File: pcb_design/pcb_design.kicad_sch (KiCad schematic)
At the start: 4 parts, among them SW1 SW_Push, SW2 SW_Push, SW3 SW_Push, U1 MOUDLE-SEEEDUINO-XIAO

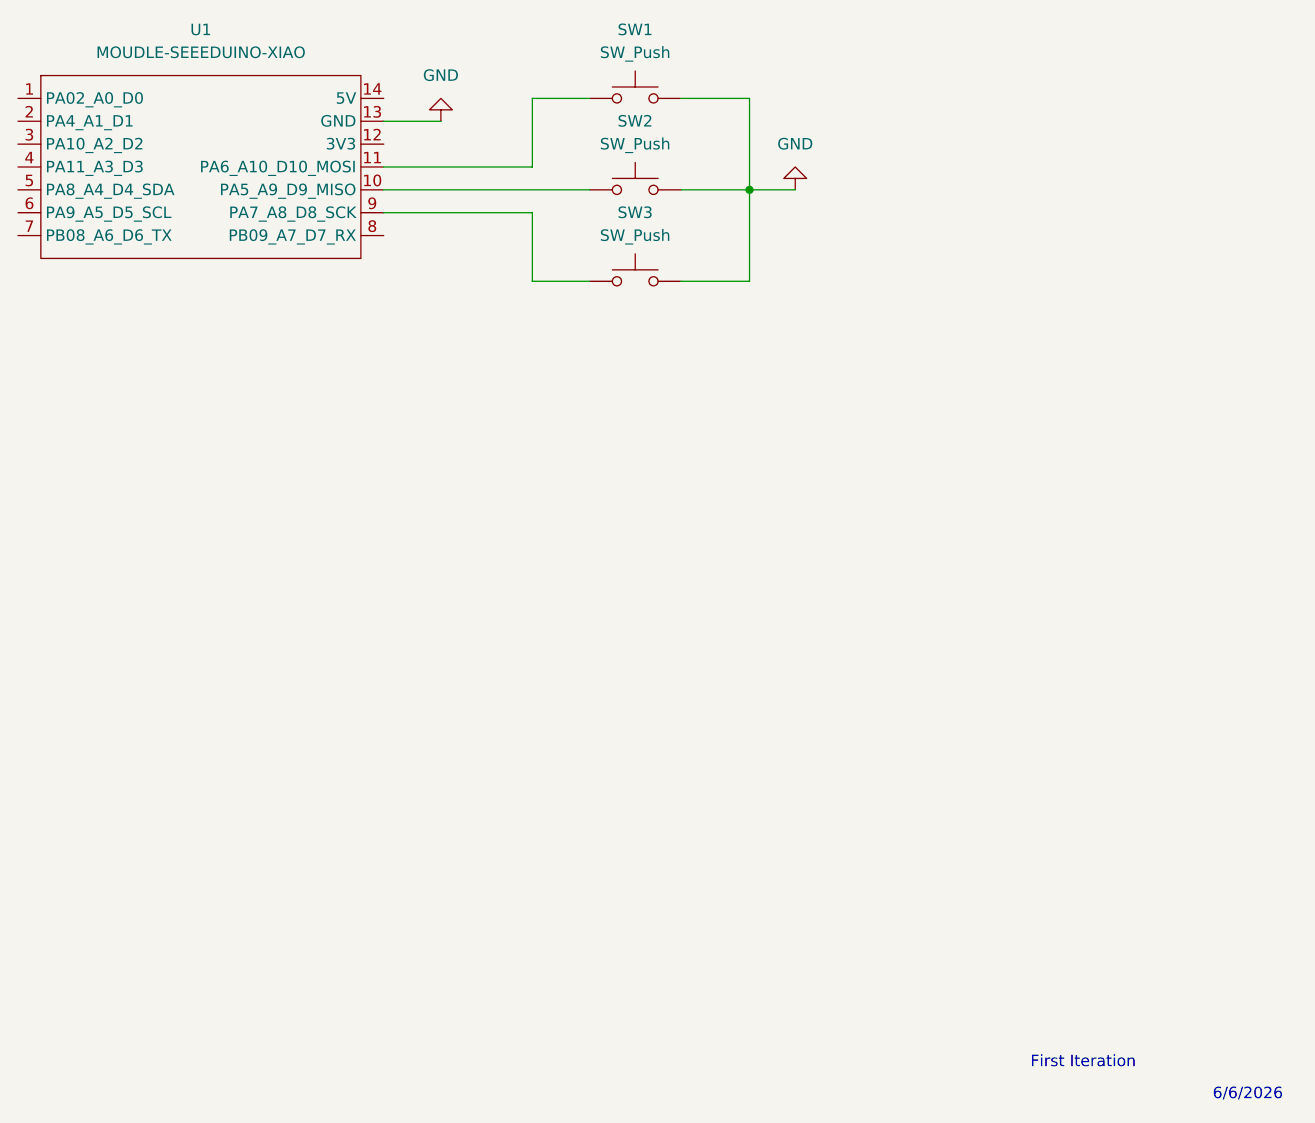
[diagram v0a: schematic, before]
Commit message: Finalized PCB Design.
1st Design Iteration - Followed the guide closely to understand the usage of KiCad.
2nd Design Iteration - Discovered the DRC function which let me fix some issues with the PCB Design
3rd Design Iteration - Redesigned the PCB to my own dimensions with a unique layout.
4th Design Iteration - Added an OLED Display to the hackpad and tested with encoder, but figured it wasn't serving a key role in my planned use case.
5th Design Iteration - Redesign the PCB to the newly discovered hackclub rules.
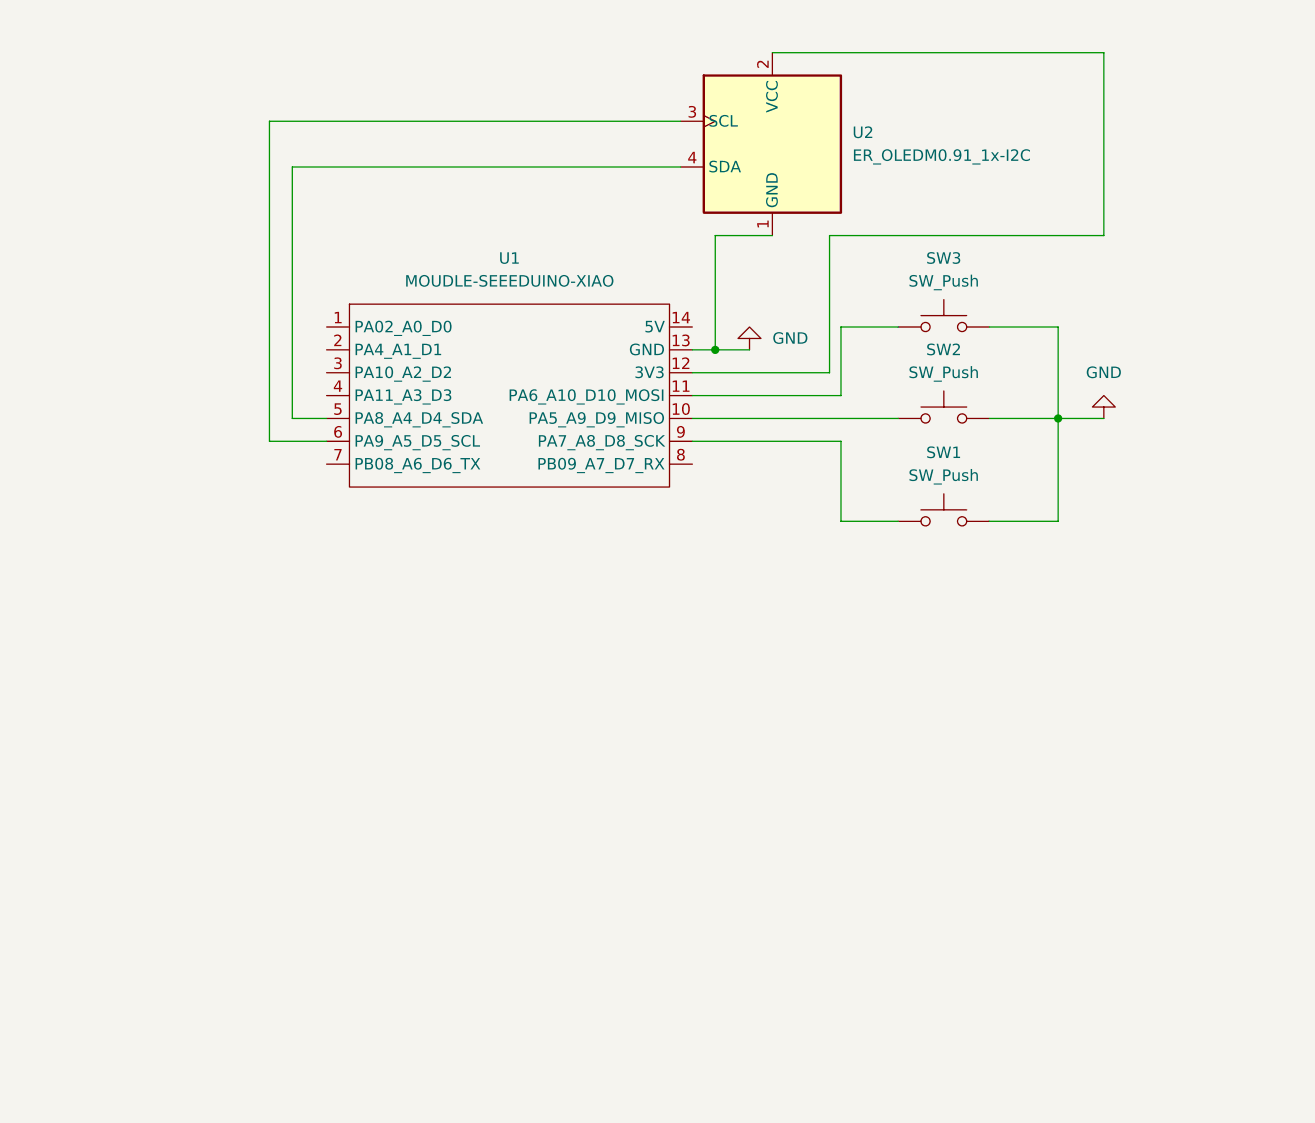
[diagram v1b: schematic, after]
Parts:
- added U2: ER_OLEDM0.91_1x-I2C, Display:ER_OLEDM0.91_1x-I2C, symbol Display_Graphic:ER_OLEDM0.91_1x-I2C
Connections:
- net GND: now also U2.1 (GND)
- net at SW3.1: now also U1.11 (PA6_A10_D10_MOSI); no longer U1.9 (PA7_A8_D8_SCK)
- net at SW1.1: now also U1.9 (PA7_A8_D8_SCK); no longer U1.11 (PA6_A10_D10_MOSI)
- net at U1.12 (3V3): now also U2.2 (VCC)
- net at U1.5 (PA8_A4_D4_SDA): now also U2.4 (SDA)
- net at U1.6 (PA9_A5_D5_SCL): now also U2.3 (SCL)
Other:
- note removed: "6/6/2026"
- note removed: "First Iteration"
- moved on the sheet: SW1, SW2, SW3, U1
